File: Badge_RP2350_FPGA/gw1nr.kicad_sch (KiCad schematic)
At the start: 24 parts, among them U2 GW1N-LV9QN88C6_I5_, U6 W25Q32JVSS

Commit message: add x to unused pins and connect more pins
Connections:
- net B17A: now also U2.31 (IOB17A)
- net B17B: now also U2.32 (IOB17B)
- no-connect marks 2 -> 49
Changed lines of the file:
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@@
+	)
+	(no_connect
+		(at 138.43 135.89)
+	)
+	(no_connect
+		(at 138.43 72.39)
+	)
+	(no_connect
+		(at 138.43 130.81)
+	)
+	(no_connect
+		(at 138.43 82.55)
+	)
+	(no_connect
+		(at 138.43 151.13)
+	)
+	(no_connect
+		(at 72.39 59.69)
+	)
+	(no_connect
+		(at 138.43 85.09)
+	)
+	(no_connect
+		(at 138.43 156.21)
+	)
+	(no_connect
+		(at 138.43 100.33)
+	)
+	(no_connect
+		(at 72.39 90.17)
+	)
+	(no_connect
+		(at 138.43 125.73)
+	)
+	(no_connect
+		(at 72.39 135.89)
+	)
+	(no_connect
+		(at 72.39 125.73)
+	)
+	(no_connect
+		(at 138.43 133.35)
+	)
+	(no_connect
+		(at 138.43 92.71)
+	)
+	(no_connect
+		(at 72.39 102.87)
+	)
+	(no_connect
+		(at 138.43 80.01)
+	)
+	(no_connect
+		(at 138.43 102.87)
+	)
+	(no_connect
+		(at 72.39 97.79)
+	)
+	(no_connect
+		(at 72.39 146.05)
+	)
+	(no_connect
+		(at 72.39 140.97)
 	)
 	(no_connect
@@
 	)
 	(no_connect
+		(at 138.43 128.27)
+	)
+	(no_connect
 		(at 234.95 134.62)
 	)
+	(no_connect
+		(at 72.39 128.27)
+	)
+	(no_connect
+		(at 72.39 95.25)
+	)
+	(no_connect
+		(at 72.39 87.63)
+	)
+	(no_connect
+		(at 72.39 62.23)
+	)
+	(no_connect
+		(at 138.43 107.95)
+	)
+	(no_connect
+		(at 138.43 87.63)
+	)
+	(no_connect
+		(at 72.39 133.35)
+	)
+	(no_connect
+		(at 72.39 130.81)
+	)
+	(no_connect
+		(at 138.43 77.47)
+	)
+	(no_connect
+		(at 138.43 148.59)
+	)
+	(no_connect
+		(at 138.43 95.25)
+	)
+	(no_connect
+		(at 72.39 148.59)
+	)
+	(no_connect
+		(at 138.43 90.17)
+	)
+	(no_connect
+		(at 138.43 97.79)
+	)
+	(no_connect
+		(at 72.39 138.43)
+	)
+	(no_connect
+		(at 138.43 138.43)
+	)
+	(no_connect
+		(at 138.43 113.03)
+	)
+	(no_connect
+		(at 138.43 143.51)
+	)
+	(no_connect
+		(at 138.43 146.05)
+	)
+	(no_connect
+		(at 138.43 140.97)
+	)
+	(no_connect
+		(at 138.43 74.93)
+	)
+	(no_connect
+		(at 138.43 105.41)
+	)
+	(no_connect
+		(at 72.39 100.33)
+	)
+	(no_connect
+		(at 72.39 143.51)
+	)
+	(no_connect
+		(at 138.43 69.85)
+	)
+	(wire
+		(pts
+			(xy 68.58 123.19) (xy 72.39 123.19)
+		)
+		(stroke
+			(width 0)
+			(type default)
+		)
+	)
 	(wire
 		(pts
@@
 		)
 		(stroke
+			(width 0)
+			(type default)
+		)
+	)
+	(wire
+		(pts
+			(xy 68.58 120.65) (xy 72.39 120.65)
+		)
+		(stroke

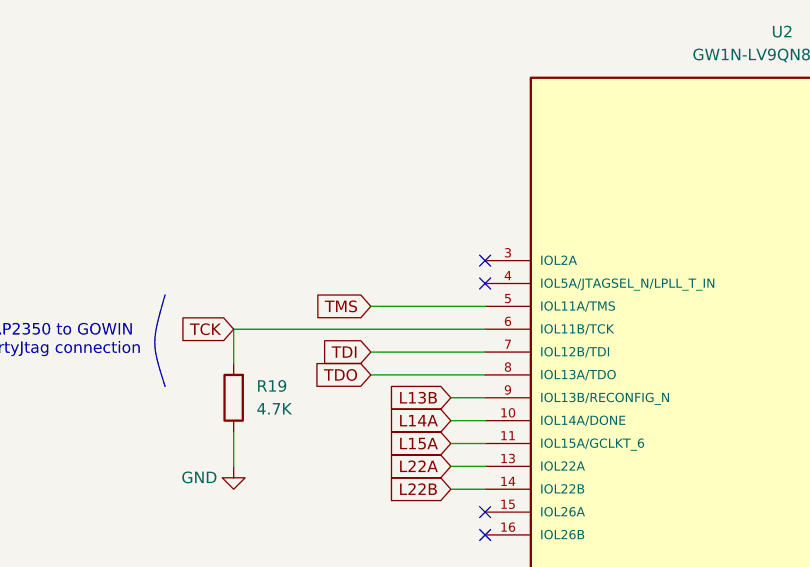
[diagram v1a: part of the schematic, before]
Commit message: add jtagsel_n connection
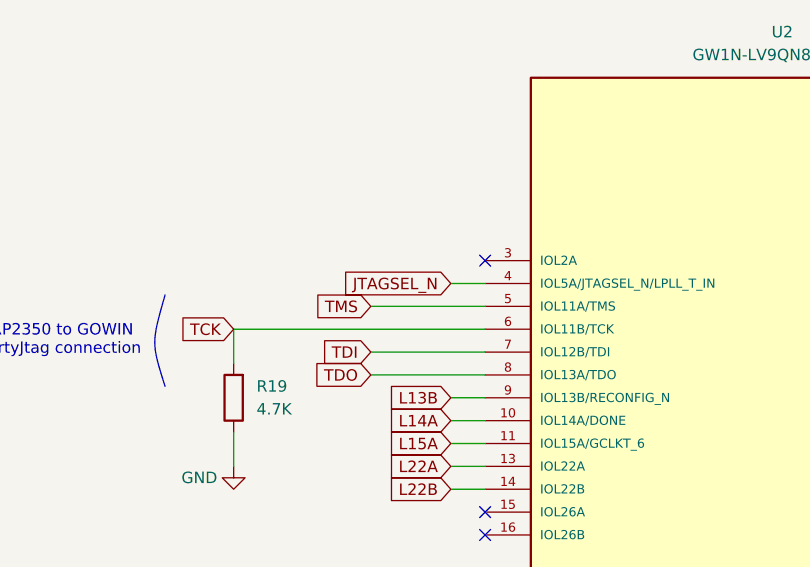
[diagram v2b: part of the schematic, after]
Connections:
- net JTAGSEL_N: now reaches U2.4 (IOL5A/JTAGSEL_N/LPLL_T_IN)
- no-connect marks 49 -> 48
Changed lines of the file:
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@@
 		(title "RISC-V Summit Europe Badge")
 		(date "2026-03-29")
-		(rev "v1.4")
+		(rev "v1.42")
 		(company "SemiTO-V, RISC-V Student Team")
 		(comment 3 "License: CERN-OHL-W-2.0")
@@
 	)
 	(no_connect
-		(at 72.39 62.23)
-	)
-	(no_connect
 		(at 138.43 107.95)
 	)
@@
 		(pts
 			(xy 227.33 31.75) (xy 227.33 41.91)
+		)
+		(stroke
+			(width 0)
+			(type default)
+		)
+	)
+	(wire
+		(pts
+			(xy 68.58 62.23) (xy 72.39 62.23)
 		)
 		(stroke
@@
 			(hide yes)
 			(show_name no)
+			(do_not_autoplace no)
+			(effects
+				(font
+					(size 1.27 1.27)
+				)
+				(justify right)
+			)
+		)
+	)
+	(global_label "JTAGSEL_N"
+		(shape input)
+		(at 68.58 62.23 180)
+		(fields_autoplaced yes)
+		(effects
+			(font
+				(size 1.27 1.27)
+			)
+			(justify right)
+		)
+		(property "Intersheetrefs" "${INTERSHEET_REFS}"
+			(at 55.6163 62.23 0)
+			(hide yes)
+			(show_name no)

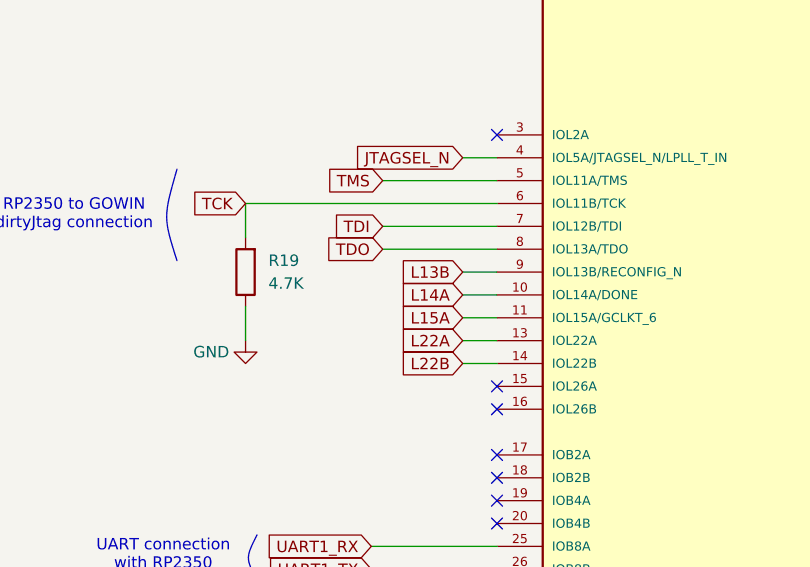
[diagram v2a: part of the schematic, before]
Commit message: add more FPGA connections and generate netlist, bom
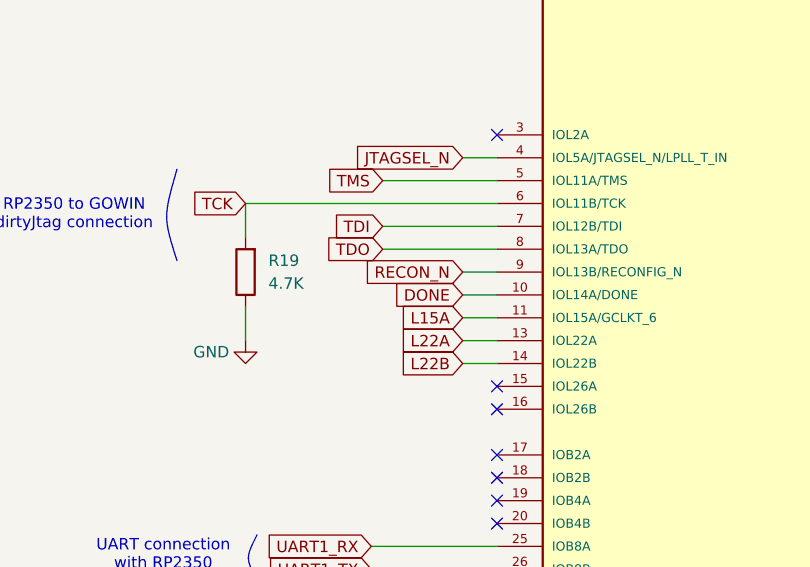
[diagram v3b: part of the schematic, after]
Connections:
- net L13B renamed RECON_N
- net L14A renamed DONE
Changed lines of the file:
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@@
 		)
 	)
-	(global_label "L14A"
+	(global_label "DONE"
 		(shape input)
 		(at 68.58 77.47 180)
@@
 		)
 		(property "Intersheetrefs" "${INTERSHEET_REFS}"
-			(at 61.0591 77.47 0)
+			(at 60.5148 77.47 0)
 			(hide yes)
 			(show_name no)
@@
 		)
 	)
-	(global_label "L13B"
+	(global_label "RECON_N"
 		(shape input)
 		(at 68.58 74.93 180)
@@
 		)
 		(property "Intersheetrefs" "${INTERSHEET_REFS}"
-			(at 60.8777 74.93 0)
+			(at 56.9467 74.93 0)
 			(hide yes)
 			(show_name no)

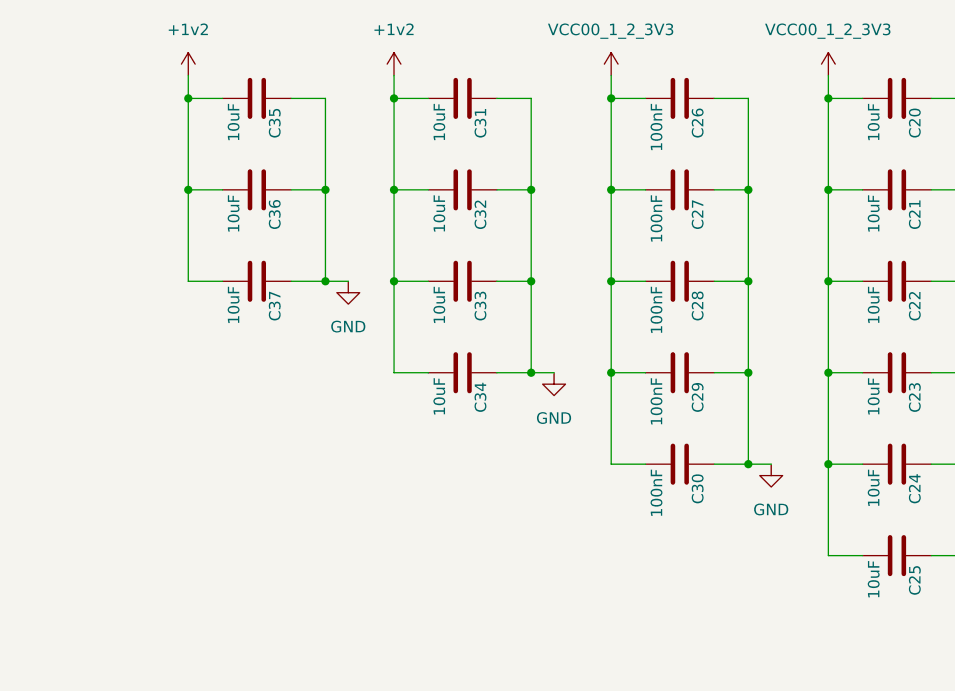
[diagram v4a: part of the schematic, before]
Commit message: M: pcb routing start, minor schematic changes
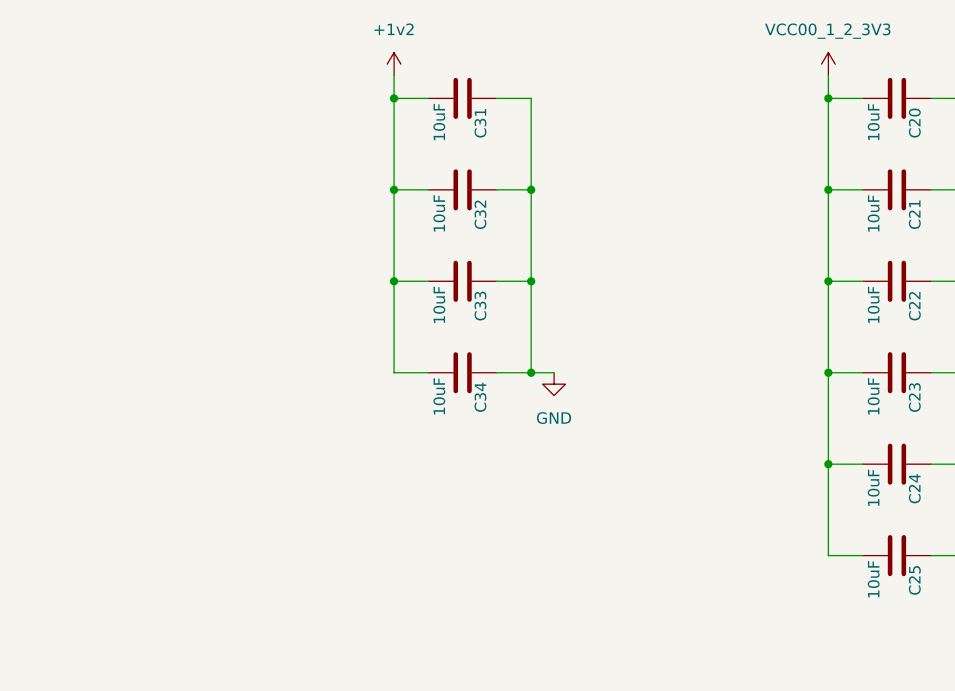
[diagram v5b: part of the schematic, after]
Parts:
- removed C26, C27, C28, C29, C30: 100nF, Capacitor_SMD:C_0402_1005Metric, symbol Device:C
- removed C35, C36, C37: 10uF, Capacitor_SMD:C_0402_1005Metric, symbol Device:C

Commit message: generate gerbers
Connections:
- net GND: now also U2.89 (EXP)
- no-connect marks 48 -> 47
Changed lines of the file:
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@@
 		(title "RISC-V Summit Europe Badge")
 		(date "2026-03-29")
-		(rev "v1.52")
+		(rev "v1.53")
 		(company "SemiTO-V, RISC-V Student Team")
 		(comment 3 "License: CERN-OHL-W-2.0")
@@
 	)
 	(junction
+		(at 142.24 158.75)
+		(diameter 0)
+		(color 0 0 0 0)
+	)
+	(junction
 		(at 275.59 62.23)
 		(diameter 0)
@@
 	)
 	(no_connect
-		(at 138.43 156.21)
-	)
-	(no_connect
 		(at 138.43 100.33)
 	)
@@
 	(wire
 		(pts
+			(xy 138.43 156.21) (xy 142.24 156.21)
+		)
+		(stroke
+			(width 0)
+			(type default)
+		)
+	)
+	(wire
+		(pts
 			(xy 232.41 132.08) (xy 234.95 132.08)
 		)
@@
 		)
 		(stroke
+			(width 0)
+			(type default)
+		)
+	)
+	(wire
+		(pts
+			(xy 142.24 156.21) (xy 142.24 158.75)
+		)
+		(stroke

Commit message: fixes
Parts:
- U2: footprint semitovpartslibrary:QFN40P1000X1000X95-89N -> Package_DFN_QFN:ArtInChip_QFN-88-1EP_10x10mm_P0.4mm_EP6.74x6.74mm_ThermalVias
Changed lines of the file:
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@@
 		(title "RISC-V Summit Europe Badge")
 		(date "2026-03-29")
-		(rev "v1.53")
+		(rev "v1.54")
 		(company "SemiTO-V, RISC-V Student Team")
 		(comment 3 "License: CERN-OHL-W-2.0")
@@
 			)
 		)
-		(property "Footprint" "semitovpartslibrary:QFN40P1000X1000X95-89N"
+		(property "Footprint" "Package_DFN_QFN:ArtInChip_QFN-88-1EP_10x10mm_P0.4mm_EP6.74x6.74mm_ThermalVias"
 			(at 105.41 100.33 0)
 			(hide yes)
